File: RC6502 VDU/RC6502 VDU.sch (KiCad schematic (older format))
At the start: 39 parts, among them J1 RC6502_Backplane, J2 VDU_BASE, J3 VIDEO, J4 Hole, J5 Hole, J6 Hole, J7 Hole, J8 RCA_PLUG, Q1 PN2222A, Q2 PN2222A, U1 MC6847, U10 74HCT00, U2 HM62256BLP-7, U3 74LS244, U4 74LS244, U5 74LS245, U6 74LS374, U7 74HCT138, U8 74HCT04, U9 74HCT00, X1 3.579545 MHz

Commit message: Assigned footprints
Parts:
- J1: footprint (none) -> Pin_Headers:Pin_Header_Angled_1x39_Pitch2.54mm
- J2: footprint (none) -> Pin_Headers:Pin_Header_Straight_1x10_Pitch2.54mm
- J3: footprint (none) -> Pin_Headers:Pin_Header_Straight_1x05_Pitch2.54mm
- J8: footprint (none) -> rca:rca_yellow
- JP1, JP2, JP3: footprint (none) -> Pin_Headers:Pin_Header_Straight_1x02_Pitch2.54mm
- R1, R2, R3, R4, R5: footprint (none) -> Resistors_THT:R_Axial_DIN0207_L6.3mm_D2.5mm_P5.08mm_Vertical
- U1: footprint (none) -> Housings_DIP:DIP-40_W15.24mm_Socket
- U10, U9: footprint (none) -> Housings_DIP:DIP-14_W7.62mm
- U3, U4, U5, U6: footprint (none) -> Housings_DIP:DIP-20_W7.62mm
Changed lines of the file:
@@
 F 0 "J1" H 10600 6350 50  0000 C CNN
 F 1 "RC6502_Backplane" V 11050 4300 50  0000 C CNN
-F 2 "" H 10600 4350 50  0001 C CNN
+F 2 "Pin_Headers:Pin_Header_Angled_1x39_Pitch2.54mm" H 10600 4350 50  0001 C CNN
 F 3 "" H 10600 4350 50  0001 C CNN
 	1    10600 4350
@@
 F 0 "U4" H 8350 2225 50  0000 C CNN
 F 1 "74LS244" H 8350 2625 50  0000 C CNN
-F 2 "" H 8350 2425 50  0001 C CNN
+F 2 "Housings_DIP:DIP-20_W7.62mm" H 8350 2425 50  0001 C CNN
 F 3 "" H 8350 2425 50  0001 C CNN
 	1    8350 2425
@@
 F 0 "U3" H 8350 1025 50  0000 C CNN
 F 1 "74LS244" H 8350 1425 50  0000 C CNN
-F 2 "" H 8350 1225 50  0001 C CNN
+F 2 "Housings_DIP:DIP-20_W7.62mm" H 8350 1225 50  0001 C CNN
 F 3 "" H 8350 1225 50  0001 C CNN
 	1    8350 1225
@@
 F 0 "U5" H 8350 4125 50  0000 C BNN
 F 1 "74LS245" H 8350 3725 50  0000 C CNN
-F 2 "" H 8350 3925 50  0001 C CNN
+F 2 "Housings_DIP:DIP-20_W7.62mm" H 8350 3925 50  0001 C CNN
 F 3 "" H 8350 3925 50  0001 C CNN
 	1    8350 3925
@@
 F 0 "J2" H 2650 1225 50  0000 C CNN
 F 1 "VDU_BASE" H 2650 625 50  0000 C CNN
-F 2 "" H 2600 925 50  0001 C CNN
+F 2 "Pin_Headers:Pin_Header_Straight_1x10_Pitch2.54mm" H 2600 925 50  0001 C CNN
 F 3 "" H 2600 925 50  0001 C CNN
 	1    2600 925
@@
 F 0 "U6" H 8350 5300 50  0000 C CNN
 F 1 "74LS374" H 8350 5500 50  0000 C CNN
-F 2 "" H 8350 5400 50  0001 C CNN
+F 2 "Housings_DIP:DIP-20_W7.62mm" H 8350 5400 50  0001 C CNN
 F 3 "" H 8350 5400 50  0001 C CNN
 	1    8350 5400
@@
 F 0 "U1" H 5600 2300 60  0000 C CNN
 F 1 "MC6847" V 5600 1950 60  0000 C CNN
-F 2 "" H 5100 2250 60  0000 C CNN
+F 2 "Housings_DIP:DIP-40_W15.24mm_Socket" H 5100 2250 60  0001 C CNN
 F 3 "" H 5100 2250 60  0000 C CNN
 	1    5600 2050
@@
 F 0 "JP2" H 3775 5855 50  0000 C CNN
 F 1 "PHI0_OUT" H 3785 5715 50  0000 C CNN
-F 2 "" H 3775 5775 50  0001 C CNN
+F 2 "Pin_Headers:Pin_Header_Straight_1x02_Pitch2.54mm" H 3775 5775 50  0001 C CNN
 F 3 "" H 3775 5775 50  0001 C CNN
 	1    3775 5775
@@
 F 0 "JP1" H 3400 1005 50  0000 C CNN
 F 1 "VDU_EN" H 3410 865 50  0000 C CNN
-F 2 "" H 3400 925 50  0001 C CNN
+F 2 "Pin_Headers:Pin_Header_Straight_1x02_Pitch2.54mm" H 3400 925 50  0001 C CNN
 F 3 "" H 3400 925 50  0001 C CNN
 	1    3400 925
@@
 F 0 "U9" H 1425 3100 50  0000 C CNN
 F 1 "74HCT00" H 1425 2950 50  0000 C CNN
-F 2 "" H 1425 3050 50  0001 C CNN
+F 2 "Housings_DIP:DIP-14_W7.62mm" H 1425 3050 50  0001 C CNN
 F 3 "" H 1425 3050 50  0001 C CNN
 	1    1425 3050
@@
 F 0 "U9" H 2850 2525 50  0000 C CNN
 F 1 "74HCT00" H 2850 2375 50  0000 C CNN
-F 2 "" H 2850 2475 50  0001 C CNN
+F 2 "Housings_DIP:DIP-14_W7.62mm" H 2850 2475 50  0001 C CNN
 F 3 "" H 2850 2475 50  0001 C CNN
 	2    2850 2475
@@
 F 0 "U9" H 2825 3575 50  0000 C CNN
 F 1 "74HCT00" H 2825 3425 50  0000 C CNN
-F 2 "" H 2825 3525 50  0001 C CNN
+F 2 "Housings_DIP:DIP-14_W7.62mm" H 2825 3525 50  0001 C CNN
 F 3 "" H 2825 3525 50  0001 C CNN
 	3    2825 3525
@@
 F 0 "U9" H 2325 4125 50  0000 C CNN
 F 1 "74HCT00" H 2325 3975 50  0000 C CNN
-F 2 "" H 2325 4075 50  0001 C CNN
+F 2 "Housings_DIP:DIP-14_W7.62mm" H 2325 4075 50  0001 C CNN
 F 3 "" H 2325 4075 50  0001 C CNN
 	4    2325 4075
@@
 F 0 "U10" H 2700 4900 50  0000 C CNN
 F 1 "74HCT00" H 2700 4750 50  0000 C CNN
-F 2 "" H 2700 4850 50  0001 C CNN
+F 2 "Housings_DIP:DIP-14_W7.62mm" H 2700 4850 50  0001 C CNN
 F 3 "" H 2700 4850 50  0001 C CNN
 	1    2700 4850
@@
 F 0 "U10" H 4625 4375 50  0000 C CNN
 F 1 "74HCT00" H 4625 4225 50  0000 C CNN
-F 2 "" H 4625 4325 50  0001 C CNN
+F 2 "Housings_DIP:DIP-14_W7.62mm" H 4625 4325 50  0001 C CNN
 F 3 "" H 4625 4325 50  0001 C CNN
 	2    4625 4325
@@
 F 0 "U10" H 4625 3875 50  0000 C CNN
 F 1 "74HCT00" H 4625 3725 50  0000 C CNN
-F 2 "" H 4625 3825 50  0001 C CNN
+F 2 "Housings_DIP:DIP-14_W7.62mm" H 4625 3825 50  0001 C CNN
 F 3 "" H 4625 3825 50  0001 C CNN
 	3    4625 3825
@@
 F 0 "U10" H 5950 4125 50  0000 C CNN
 F 1 "74HCT00" H 5950 3975 50  0000 C CNN
-F 2 "" H 5950 4075 50  0001 C CNN
+F 2 "Housings_DIP:DIP-14_W7.62mm" H 5950 4075 50  0001 C CNN
 F 3 "" H 5950 4075 50  0001 C CNN
 	4    5950 4075
@@
 F 0 "JP3" H 9375 4505 50  0000 C CNN
 F 1 "INT_ON_FS" H 9385 4365 50  0000 C CNN
-F 2 "" H 9375 4425 50  0001 C CNN
+F 2 "Pin_Headers:Pin_Header_Straight_1x02_Pitch2.54mm" H 9375 4425 50  0001 C CNN
 F 3 "" H 9375 4425 50  0001 C CNN
 	1    9375 4425
@@
 F 0 "J3" H 4675 3625 50  0000 C CNN
 F 1 "VIDEO" H 4675 3025 50  0000 C CNN
-F 2 "" H 4675 3325 50  0001 C CNN
+F 2 "Pin_Headers:Pin_Header_Straight_1x05_Pitch2.54mm" H 4675 3325 50  0001 C CNN
 F 3 "" H 4675 3325 50  0001 C CNN
 	1    4675 3325
@@
 F 0 "R5" V 6505 5325 50  0000 C CNN
 F 1 "1k" V 6425 5325 50  0000 C CNN
-F 2 "" V 6355 5325 50  0001 C CNN
+F 2 "Resistors_THT:R_Axial_DIN0207_L6.3mm_D2.5mm_P5.08mm_Vertical" V 6355 5325 50  0001 C CNN
 F 3 "" H 6425 5325 50  0001 C CNN
 	1    6425 5325
@@
 F 0 "R3" V 6005 5925 50  0000 C CNN
 F 1 "180" V 5925 5925 50  0000 C CNN
-F 2 "" V 5855 5925 50  0001 C CNN
+F 2 "Resistors_THT:R_Axial_DIN0207_L6.3mm_D2.5mm_P5.08mm_Vertical" V 5855 5925 50  0001 C CNN
 F 3 "" H 5925 5925 50  0001 C CNN
 	1    5925 5925
@@
 F 0 "R4" V 6055 5325 50  0000 C CNN
 F 1 "6.2k" V 5975 5325 50  0000 C CNN
-F 2 "" V 5905 5325 50  0001 C CNN
+F 2 "Resistors_THT:R_Axial_DIN0207_L6.3mm_D2.5mm_P5.08mm_Vertical" V 5905 5325 50  0001 C CNN
 F 3 "" H 5975 5325 50  0001 C CNN
 	1    5975 5325
@@
 F 0 "R2" V 5830 5100 50  0000 C CNN
 F 1 "1k" V 5750 5100 50  0000 C CNN
-F 2 "" V 5680 5100 50  0001 C CNN
+F 2 "Resistors_THT:R_Axial_DIN0207_L6.3mm_D2.5mm_P5.08mm_Vertical" V 5680 5100 50  0001 C CNN
 F 3 "" H 5750 5100 50  0001 C CNN
 	1    5750 5100
@@
 F 0 "R1" V 5205 6075 50  0000 C CNN
 F 1 "1k" V 5125 6075 50  0000 C CNN
-F 2 "" V 5055 6075 50  0001 C CNN
+F 2 "Resistors_THT:R_Axial_DIN0207_L6.3mm_D2.5mm_P5.08mm_Vertical" V 5055 6075 50  0001 C CNN
 F 3 "" H 5125 6075 50  0001 C CNN
 	1    5125 6075
@@
 F 0 "J8" H 4910 5970 50  0000 C CNN
 F 1 "RCA_PLUG" V 5015 5850 50  0000 C CNN
-F 2 "" H 4900 5850 50  0001 C CNN
+F 2 "rca:rca_yellow" H 4900 5850 50  0001 C CNN
 F 3 "" H 4900 5850 50  0001 C CNN
 	1    4900 5850

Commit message: Fixed footprint error
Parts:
- J4, J5, J6, J7: footprint rc6502:Mounting -> mounting:Mounting
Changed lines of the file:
@@
 F 0 "J4" V 10350 1975 50  0000 C CNN
 F 1 "Hole" V 10350 1975 50  0001 C CNN
-F 2 "rc6502:Mounting" H 10250 1975 50  0001 C CNN
+F 2 "mounting:Mounting" H 10250 1975 50  0001 C CNN
 F 3 "" H 10250 1975 50  0001 C CNN
 	1    10250 1975
@@
 F 0 "J6" V 10600 1975 50  0000 C CNN
 F 1 "Hole" V 10600 1975 50  0001 C CNN
-F 2 "rc6502:Mounting" H 10500 1975 50  0001 C CNN
+F 2 "mounting:Mounting" H 10500 1975 50  0001 C CNN
 F 3 "" H 10500 1975 50  0001 C CNN
 	1    10500 1975
@@
 F 0 "J5" V 10475 1975 50  0000 C CNN
 F 1 "Hole" V 10475 1975 50  0001 C CNN
-F 2 "rc6502:Mounting" H 10375 1975 50  0001 C CNN
+F 2 "mounting:Mounting" H 10375 1975 50  0001 C CNN
 F 3 "" H 10375 1975 50  0001 C CNN
 	1    10375 1975
@@
 F 0 "J7" V 10725 1975 50  0000 C CNN
 F 1 "Hole" V 10725 1975 50  0001 C CNN
-F 2 "rc6502:Mounting" H 10625 1975 50  0001 C CNN
+F 2 "mounting:Mounting" H 10625 1975 50  0001 C CNN
 F 3 "" H 10625 1975 50  0001 C CNN
 	1    10625 1975

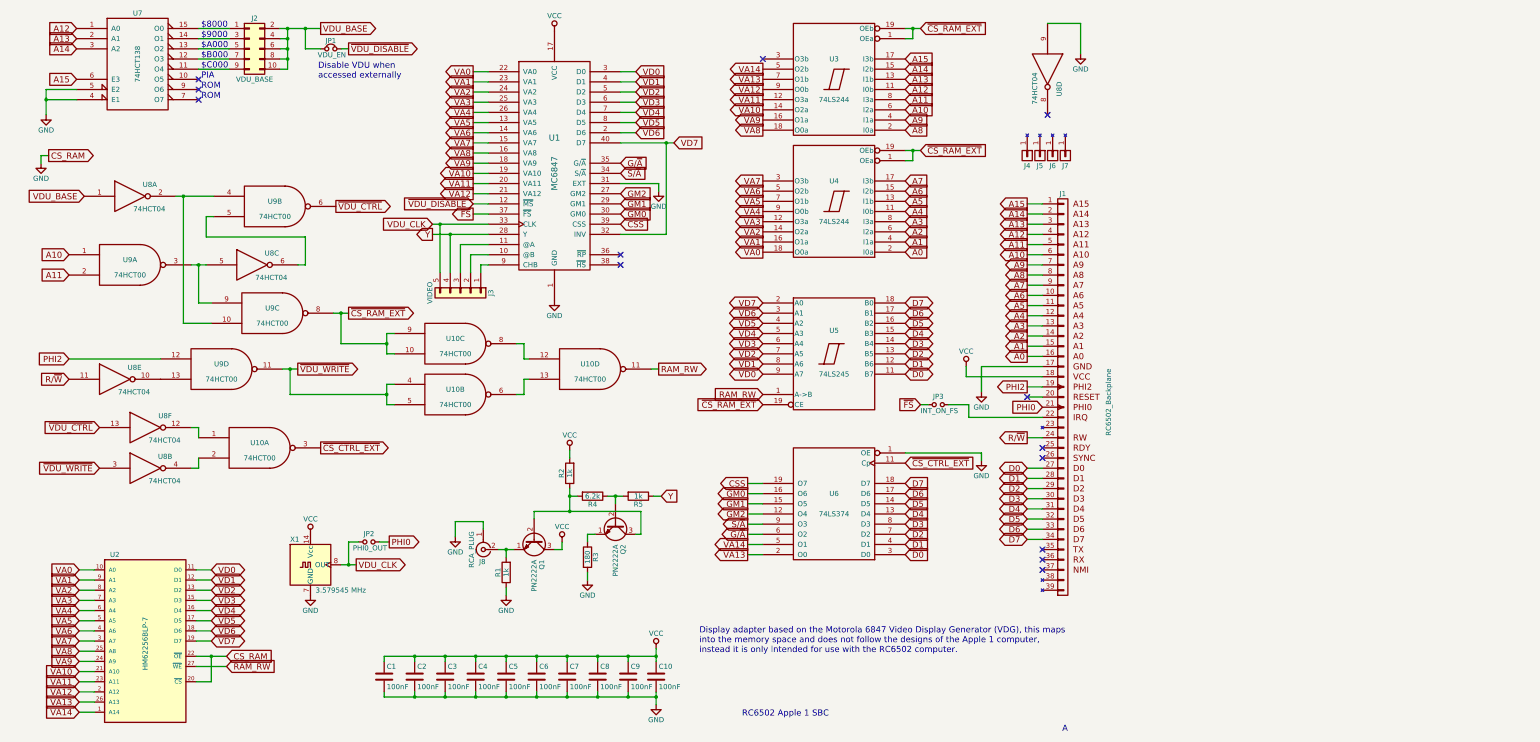
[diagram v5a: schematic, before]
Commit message: Forced KiCad to actually use GND as ground name
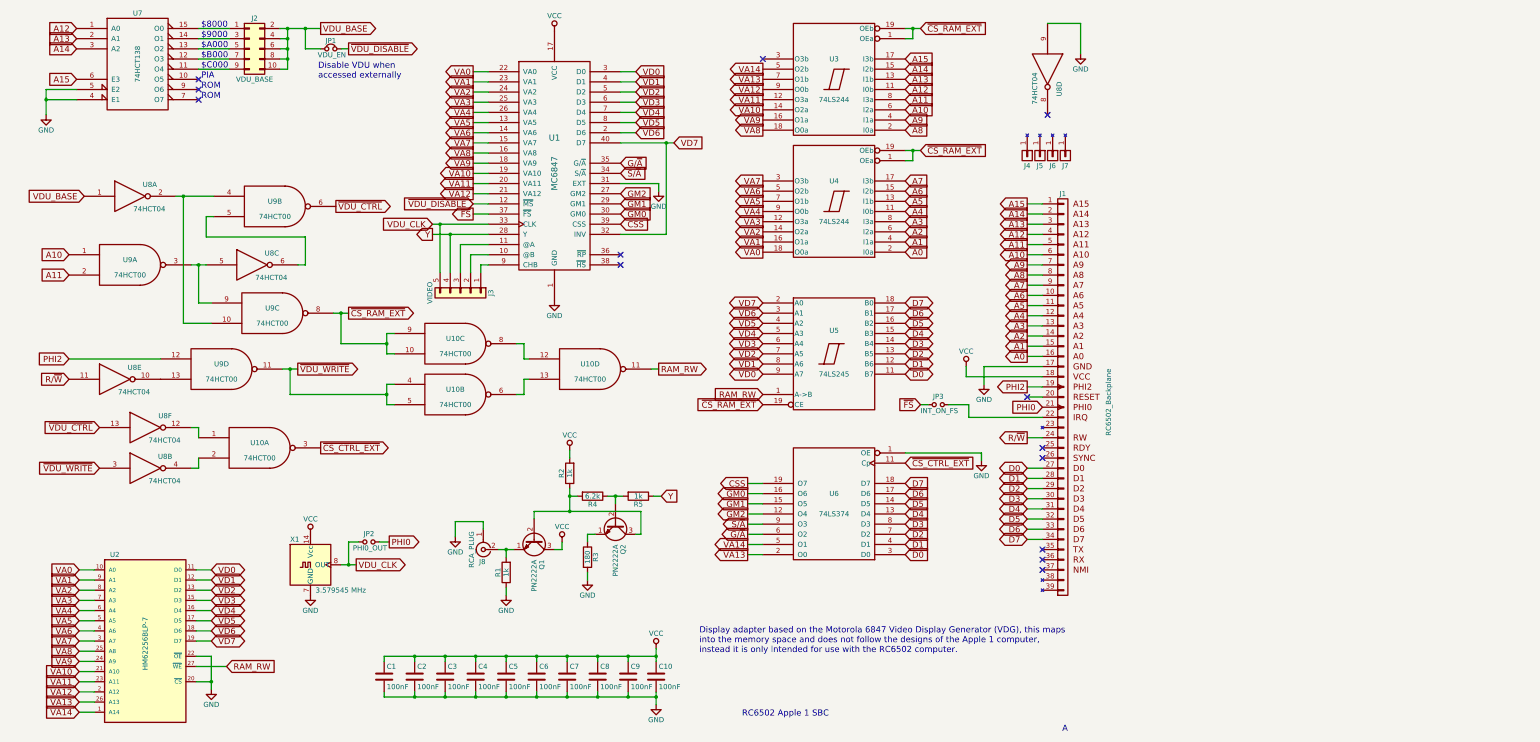
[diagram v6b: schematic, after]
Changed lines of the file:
@@
 	900  1325 600  1325
 Wire Wire Line
-	600  1325 600  1575
+	600  1325 600  1425
+Wire Wire Line
+	600  1425 600  1575
 Wire Wire Line
 	900  1425 600  1425
@@
 $EndComp
 Wire Wire Line
-	3925 6900 6600 6900
+	3925 6900 4225 6900
+Wire Wire Line
+	4225 6900 4525 6900
+Wire Wire Line
+	4525 6900 4825 6900
+Wire Wire Line
+	4825 6900 5125 6900
+Wire Wire Line
+	5125 6900 5425 6900
+Wire Wire Line
+	5425 6900 5725 6900
+Wire Wire Line
+	5725 6900 6025 6900
+Wire Wire Line
+	6025 6900 6325 6900
+Wire Wire Line
+	6325 6900 6600 6900
 Wire Wire Line
 	4225 6900 4225 6950
@@
 	4225 7250 4225 7300
 Wire Wire Line
-	3925 7300 6600 7300
+	3925 7300 4225 7300
+Wire Wire Line
+	4225 7300 4525 7300
+Wire Wire Line
+	4525 7300 4825 7300
+Wire Wire Line
+	4825 7300 5125 7300
+Wire Wire Line
+	5125 7300 5425 7300
+Wire Wire Line
+	5425 7300 5725 7300
+Wire Wire Line
+	5725 7300 6025 7300
+Wire Wire Line
+	6025 7300 6325 7300
+Wire Wire Line
+	6325 7300 6600 7300
 Connection ~ 6025 7300
 Wire Wire Line
@@
 	1    0    0    -1
 $EndComp
-$Comp
-L GND #PWR02
-U 1 1 5C04B599
-P 9800 4300
-F 0 "#PWR02" H 9800 4050 50  0001 C CNN
-F 1 "GND" H 9800 4150 50  0000 C CNN
-F 2 "" H 9800 4300 50  0001 C CNN
-F 3 "" H 9800 4300 50  0001 C CNN
-	1    9800 4300
-	1    0    0    -1
-$EndComp
 NoConn ~ 10400 6050
 NoConn ~ 10400 4850
 NoConn ~ 10400 4950
-Wire Wire Line
-	9800 4300 9800 4050
-Wire Wire Line
-	9800 4050 10400 4050
 Wire Wire Line
 	10250 2450 10400 2450
@@
 NoConn ~ 2100 1425
 Wire Wire Line
-	2900 725  3300 725
-Wire Wire Line
-	2975 725  2975 1125
+	2900 725  2975 725
+Wire Wire Line
+	2975 725  3150 725
+Wire Wire Line
+	3150 725  3300 725
+Wire Wire Line
+	2975 725  2975 825
+Wire Wire Line
+	2975 825  2975 925
+Wire Wire Line
+	2975 925  2975 1025
+Wire Wire Line
+	2975 1025 2975 1125
 Wire Wire Line
 	2975 1125 2900 1125
@@
 VDU_CLK
 Wire Wire Line
-	3500 6000 3650 6000
-$Comp
-L GND #PWR03
+	3500 6000 3575 6000
+Wire Wire Line
+	3575 6000 3650 6000
+$Comp
+L GND #PWR02
 U 1 1 5C0463DB
 P 3200 6300
-F 0 "#PWR03" H 3200 6050 50  0001 C CNN
+F 0 "#PWR02" H 3200 6050 50  0001 C CNN
 F 1 "GND" H 3200 6150 50  0000 C CNN
 F 2 "" H 3200 6300 50  0001 C CNN
@@
 $EndComp
 $Comp
-L VCC #PWR04
+L VCC #PWR03
 U 1 1 5C0465FA
 P 3200 5700
-F 0 "#PWR04" H 3200 5550 50  0001 C CNN
+F 0 "#PWR03" H 3200 5550 50  0001 C CNN
 F 1 "VCC" H 3200 5850 50  0000 C CNN
 F 2 "" H 3200 5700 50  0001 C CNN
@@
 $EndComp
 $Comp
-L VCC #PWR05
+L VCC #PWR04
 U 1 1 5C046B61
 P 6600 6825
-F 0 "#PWR05" H 6600 6675 50  0001 C CNN
+F 0 "#PWR04" H 6600 6675 50  0001 C CNN
 F 1 "VCC" H 6600 6975 50  0000 C CNN
 F 2 "" H 6600 6825 50  0001 C CNN
@@
 $EndComp
 $Comp
-L GND #PWR06
+L GND #PWR05
 U 1 1 5C046BC0
 P 6600 7375
-F 0 "#PWR06" H 6600 7125 50  0001 C CNN
+F 0 "#PWR05" H 6600 7125 50  0001 C CNN
 F 1 "GND" H 6600 7225 50  0000 C CNN
 F 2 "" H 6600 7375 50  0001 C CNN
@@
 D0
 $Comp
-L GND #PWR07
+L GND #PWR06
 U 1 1 5C04D9C7
 P 600 1575
-F 0 "#PWR07" H 600 1325 50  0001 C CNN
+F 0 "#PWR06" H 600 1325 50  0001 C CNN
 F 1 "GND" H 600 1425 50  0000 C CNN
 F 2 "" H 600 1575 50  0001 C CNN
@@
 $EndComp
 $Comp
-L GND #PWR08
+L GND #PWR07
 U 1 1 5C04E709
 P 9800 4975
-F 0 "#PWR08" H 9800 4725 50  0001 C CNN
+F 0 "#PWR07" H 9800 4725 50  0001 C CNN
 F 1 "GND" H 9800 4825 50  0000 C CNN
 F 2 "" H 9800 4975 50  0001 C CNN
@@
 	6250 1750 6400 1750
 Wire Wire Line
-	6250 1850 6775 1850
+	6250 1850 6700 1850
+Wire Wire Line
+	6700 1850 6775 1850
 Wire Wire Line
 	6250 1650 6400 1650
@@
 VDU_CLK
 Wire Wire Line
-	4400 2650 4950 2650
+	4400 2650 4475 2650
+Wire Wire Line
+	4475 2650 4950 2650
 Wire Wire Line
 	4800 1750 4950 1750
@@
 	3875 5775 3975 5775
 $Comp
-L GND #PWR09
+L GND #PWR08
 U 1 1 5C0636E6
 P 5600 3400
-F 0 "#PWR09" H 5600 3150 50  0001 C CNN
+F 0 "#PWR08" H 5600 3150 50  0001 C CNN
 F 1 "GND" H 5600 3250 50  0000 C CNN
 F 2 "" H 5600 3400 50  0001 C CNN
@@
 	7650 5700 7500 5700
 $Comp
-L GND #PWR010
+L GND #PWR09
 U 1 1 5C06A7C5
 P 6625 2325
-F 0 "#PWR010" H 6625 2075 50  0001 C CNN
+F 0 "#PWR09" H 6625 2075 50  0001 C CNN
 F 1 "GND" H 6625 2175 50  0000 C CNN
 F 2 "" H 6625 2325 50  0001 C CNN
@@
 	6625 2250 6625 2325
 $Comp
-L VCC #PWR011
+L VCC #PWR010
 U 1 1 5C06AFB8
 P 5600 750
-F 0 "#PWR011" H 5600 600 50  0001 C CNN
+F 0 "#PWR010" H 5600 600 50  0001 C CNN
 F 1 "VCC" H 5600 900 50  0000 C CNN
 F 2 "" H 5600 750 50  0001 C CNN
@@
 ~CS_RAM_EXT
 Wire Wire Line
-	9050 725  9200 725
+	9050 725  9125 725
+Wire Wire Line
+	9125 725  9200 725
 Wire Wire Line
 	9125 725  9125 825
@@
 ~CS_RAM_EXT
 Wire Wire Line
-	9050 1925 9200 1925
+	9050 1925 9125 1925
+Wire Wire Line
+	9125 1925 9200 1925
 Wire Wire Line
 	9125 1925 9125 2025
@@
 RAM_RW
 Wire Wire Line
-	2075 6900 2375 6900
+	2075 6900 2225 6900
 Wire Wire Line
 	2375 7000 2075 7000
@@
 $EndComp
 $Comp
-L GND #PWR012
+L GND #PWR011
 U 1 1 5C0ADFE0
 P 10775 975
-F 0 "#PWR012" H 10775 725 50  0001 C CNN
+F 0 "#PWR011" H 10775 725 50  0001 C CNN
 F 1 "GND" H 10775 825 50  0000 C CNN
 F 2 "" H 10775 975 50  0001 C CNN
@@
 	2075 7150 2225 7150
 Wire Wire Line
-	2225 7150 2225 6900
-Connection ~ 2225 6900
-Text GLabel 2375 6900 2    60   Input ~ 0
-CS_RAM
-Text GLabel 625  1975 2    60   Output ~ 0
-CS_RAM
-$Comp
-L GND #PWR013
-U 1 1 5C0AFC48
-P 550 2050
-F 0 "#PWR013" H 550 1800 50  0001 C CNN
-F 1 "GND" H 550 1900 50  0000 C CNN
-F 2 "" H 550 2050 50  0001 C CNN
-F 3 "" H 550 2050 50  0001 C CNN
-	1    550  2050
-	1    0    0    -1
-$EndComp
-Wire Wire Line
-	550  2050 550  1975
-Wire Wire Line
-	550  1975 625  1975
+	2225 6900 2225 7150
+Wire Wire Line
+	2225 7150 2225 7225
 NoConn ~ 10250 4350
 $Comp
@@
 R/~W
 Wire Wire Line
-	2025 3050 2175 3050
+	2025 3050 2100 3050
+Wire Wire Line
+	2100 3050 2175 3050
 Wire Wire Line
 	2250 2575 2175 2575
@@
 	1950 3625 1950 2375
 Wire Wire Line
-	1875 2375 2250 2375
+	1875 2375 1950 2375
+Wire Wire Line
+	1950 2375 2250 2375
 Connection ~ 1950 2375
 Text GLabel 3575 3525 2    60   Output ~ 0
@@
 ~VDU_WRITE
 Wire Wire Line
-	3425 3525 3575 3525
-Wire Wire Line
-	2925 4075 3075 4075
+	3425 3525 3500 3525
+Wire Wire Line
+	3500 3525 3575 3525
+Wire Wire Line
+	2925 4075 3000 4075
+Wire Wire Line
+	3000 4075 3075 4075
 Wire Wire Line
 	3000 4075 3000 4325
@@
 $EndComp
 Wire Wire Line
-	6600 7250 6600 7375
+	6600 7250 6600 7300
+Wire Wire Line
+	6600 7300 6600 7375
 Connection ~ 6600 7300
 Wire Wire Line
-	6600 6825 6600 6950
+	6600 6825 6600 6900
+Wire Wire Line
+	6600 6900 6600 6950
 Connection ~ 6600 6900
 Wire Wire Line
@@
 	3950 3925 4025 3925
 Wire Wire Line
-	3950 3725 3950 3925
+	3950 3725 3950 3825
+Wire Wire Line
+	3950 3825 3950 3925
 Wire Wire Line
 	3950 3725 4025 3725
@@
 	3950 4425 4025 4425
 Wire Wire Line
-	3950 4225 3950 4425
+	3950 4225 3950 4325
+Wire Wire Line
+	3950 4325 3950 4425
 Wire Wire Line
 	3950 4225 4025 4225
@@
 	4575 3125 4575 2750
 Wire Wire Line
-	4400 2750 4950 2750
+	4400 2750 4575 2750
+Wire Wire Line
+	4575 2750 4950 2750
 Wire Wire Line
 	4475 3125 4475 2650
@@
 	6575 5325 6650 5325
 Wire Wire Line
-	6125 5325 6275 5325
+	6125 5325 6200 5325
+Wire Wire Line
+	6200 5325 6275 5325
 Wire Wire Line
 	6200 5325 6200 5400
@@
 $EndComp
 $Comp
-L GND #PWR014
+L GND #PWR013
 U 1 1 5C0DA1BF
 P 5925 6150
-F 0 "#PWR014" H 5925 5900 50  0001 C CNN
+F 0 "#PWR013" H 5925 5900 50  0001 C CNN
 F 1 "GND" H 5925 6000 50  0000 C CNN
 F 2 "" H 5925 6150 50  0001 C CNN
@@
 Connection ~ 6200 5325
 $Comp
-L VCC #PWR015
+L VCC #PWR014
 U 1 1 5C0DBAFF
 P 5750 4875
-F 0 "#PWR015" H 5750 4725 50  0001 C CNN
+F 0 "#PWR014" H 5750 4725 50  0001 C CNN
 F 1 "VCC" H 5750 5025 50  0000 C CNN
 F 2 "" H 5750 4875 50  0001 C CNN
@@
 	6450 5700 6450 5475
 Wire Wire Line
-	6450 5475 5400 5475
-Wire Wire Line
-	5750 5250 5750 5475
+	6450 5475 5750 5475
+Wire Wire Line
+	5750 5475 5400 5475
+Wire Wire Line
+	5750 5250 5750 5325
+Wire Wire Line
+	5750 5325 5750 5475
 Wire Wire Line
 	5750 5325 5825 5325
@@
 Connection ~ 5750 5475
 $Comp
-L VCC #PWR016
+L VCC #PWR015
 U 1 1 5C0DD54D
 P 5675 5775
-F 0 "#PWR016" H 5675 5625 50  0001 C CNN
+F 0 "#PWR015" H 5675 5625 50  0001 C CNN
 F 1 "VCC" H 5675 5925 50  0000 C CNN
 F 2 "" H 5675 5775 50  0001 C CNN
@@
 	5125 5925 5125 5850
 Wire Wire Line
-	5050 5850 5200 5850
+	5050 5850 5125 5850
+Wire Wire Line
+	5125 5850 5200 5850
 Wire Wire Line
 	5125 6225 5125 6300
 $Comp
-L GND #PWR017
+L GND #PWR016
 U 1 1 5C0DE051
 P 5125 6300
-F 0 "#PWR017" H 5125 6050 50  0001 C CNN
+F 0 "#PWR016" H 5125 6050 50  0001 C CNN
 F 1 "GND" H 5125 6150 50  0000 C CNN
 F 2 "" H 5125 6300 50  0001 C CNN
@@
 Connection ~ 5125 5850
 $Comp
-L GND #PWR018
+L GND #PWR017
 U 1 1 5C0DF101
 P 4625 5725
-F 0 "#PWR018" H 4625 5475 50  0001 C CNN
+F 0 "#PWR017" H 4625 5475 50  0001 C CNN
 F 1 "GND" H 4625 5575 50  0000 C CNN
 F 2 "" H 4625 5725 50  0001 C CNN
@@
 Text Notes 7025 6875 0    60   ~ 0
 Display adapter based on the Motorola 6847 Video Display Generator (VDG), this maps\ninto the memory space and does not follow the designs of the Apple 1 computer,\ninstead it is only intended for use with the RC6502 computer.
+Wire Wire Line
+	9825 4050 10400 4050
+$Comp
+L GND #PWR?
+U 1 1 5C0ECDB6
+P 2225 7225
+F 0 "#PWR?" H 2225 6975 50  0001 C CNN
+F 1 "GND" H 2225 7075 50  0000 C CNN
+F 2 "" H 2225 7225 50  0001 C CNN
+F 3 "" H 2225 7225 50  0001 C CNN
+	1    2225 7225
+	1    0    0    -1
+$EndComp
+Connection ~ 2225 7150
+Wire Wire Line
+	9825 4050 9825 4225
+$Comp
+L GND #PWR?
+U 1 1 5C0EE352
+P 9825 4225
+F 0 "#PWR?" H 9825 3975 50  0001 C CNN
+F 1 "GND" H 9825 4075 50  0000 C CNN
+F 2 "" H 9825 4225 50  0001 C CNN
+F 3 "" H 9825 4225 50  0001 C CNN
+	1    9825 4225
+	1    0    0    -1
+$EndComp
 $EndSCHEMATC
